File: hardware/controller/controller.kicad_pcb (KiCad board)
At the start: 4 copper layers, 100 x 60 mm, 210 parts, among them J1 USB_C_Receptacle_USB2.0_14P, J10 Conn_01x01, J11 Conn_01x01, J12 Conn_01x01, J13 Conn_01x06, J14 Conn_01x03, J15 Mini-SPOX, J16 Mini-SPOX, J2 IDC-10, J3 XT-60, J4 Conn_01x07, J5 Conn_01x01, J6 Conn_01x01, J7 Conn_01x01, J8 Conn_01x06, J9 Conn_01x03, Q1 AOD4189, Q10 AOD66406, Q11 AOD66406, Q12 AOD66406, Q13 AOD66406, Q2 AOD66406, Q3 AOD66406, Q4 AOD66406, Q5 AOD66406, Q6 AOD66406, Q7 AOD66406, Q8 AOD66406, Q9 AOD66406, SW1 SW_Push, SW2 SW_SPST, U1 USBLC6-2SC6, U10 MCP6541, U11 LM2105D, U12 MCP6541, U13 LM2105D, U14 MCP6541, U15 LM2105D, U16 MCP6541, U17 LM2105D, U18 MCP6541, U19 LM2105D, U2 STM32H523RETx, U20 TXS0101DBV, U21 TXS0101DBV, U3 ESP32-C3-WROOM-02, U4 LM1117MP-3.3, U5 LV14340, U6 MPU-6050, U7 HMC5883L, U8 MCP6541, U9 LM2105D, Y1 8MHz

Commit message: wip - placement
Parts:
- removed J15, J16: Mini-SPOX, hogger2:Molex-MiniSPOX-22057035-5268
- C10, C11, C12, C13, C14, C15, C21, C22, C23, C24, C25, C26, C27, C28, C29, C36, C37, C38, C39, C40, C41, C42, C44, C45, C46, C47, C49, C50, C51, C52, C54, C55, C56, C57, C59, C60, C61, C62, C64, C65, C66, C67, C69, C70, C73, C74, D3, JP1, JP2, JP3, JP4, JP5, JP6, L1, R10, R12, R14, R15, R16, R20, R21, R22, R23, R24, R25, R26, R27, R28, R29, R30, R31, R32, R33, R34, R35, R36, R37, R38, R39, R40, R41, R42, R43, R44, R45, R46, R47, R48, R49, R50, R51, R52, R53, R54, R55, R56, R57, R58, R59, R60, R61, R62, R63, U10, U11, U12, U13, U14, U15, U16, U17, U18, U19, U20, U21, U3, U4, U5, U7, U8, U9: moved to B.Cu
- J12: value Conn_01x01 -> Conn_01x09; footprint Connector_Wire:SolderWire-2.5sqmm_1x01_D2.4mm_OD4.4mm -> Connector_PinHeader_2.54mm:PinHeader_1x09_P2.54mm_Vertical
- J13: value Conn_01x06 -> Mini-SPOX; footprint Connector_PinHeader_2.54mm:PinHeader_1x06_P2.54mm_Vertical -> hogger2:Molex-MiniSPOX-22057035-5268
- J14: value Conn_01x03 -> Mini-SPOX; footprint Connector_PinHeader_2.54mm:PinHeader_1x03_P2.54mm_Vertical -> hogger2:Molex-MiniSPOX-22057035-5268
- J8: value Conn_01x06 -> Conn_01x09; footprint Connector_PinHeader_2.54mm:PinHeader_1x06_P2.54mm_Vertical -> Connector_PinHeader_2.54mm:PinHeader_1x09_P2.54mm_Vertical
- J9: value Conn_01x03 -> Conn_01x01; footprint Connector_PinHeader_2.54mm:PinHeader_1x03_P2.54mm_Vertical -> Connector_Wire:SolderWire-2.5sqmm_1x01_D2.4mm_OD4.4mm
- moved U7 176.1 mm to (146.5, 53.5)
- moved C69 173.0 mm to (131.2, 107.0), turned to 90 degrees
- moved C70 173.0 mm to (131.2, 111.0), turned to -90 degrees
- moved R21 171.9 mm to (141.5, 55.5), turned to 180 degrees
- moved R20 169.6 mm to (141.5, 57.5), turned to 180 degrees
- moved C36 168.1 mm to (141.5, 53.5), turned to 180 degrees
- moved J13 168.1 mm to (135.5, 113.5)
- moved C72 167.3 mm to (137.0, 109.5)
- moved C37 162.0 mm to (150.5, 53.2), turned to -90 degrees
- moved C38 161.3 mm to (152.5, 54.0), turned to -90 degrees
- moved U20 161.1 mm to (134.2, 109.0), turned to -90 degrees
- moved C73 144.6 mm to (160.0, 107.0), turned to 90 degrees
- moved C74 144.5 mm to (160.0, 111.0), turned to -90 degrees
- moved JP1 142.8 mm to (111.5, 85.5), turned to 90 degrees
- moved U8 141.7 mm to (107.5, 87.5), turned to 90 degrees
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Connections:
- J10 pad 1: /motor2/PHASE_U -> /motor2/PHASE_V
- J11 pad 1: /motor2/PHASE_V -> /motor2/PHASE_W
- J12 pad 1: /motor2/PHASE_W -> MOTOR2_PWM_UH
- J13 pad 1: MOTOR2_PWM_UH -> GND
- J13 pad 2: MOTOR2_PWM_UL -> VBUS
- J13 pad 3: MOTOR2_PWM_VH -> /servos/SERVO1_TTL
- J14 pad 1: MOTOR2_BEMF_U -> GND
- J14 pad 2: MOTOR2_BEMF_V -> VBUS
- J14 pad 3: MOTOR2_BEMF_W -> /servos/SERVO2_TTL
- J9 pad 1: MOTOR1_BEMF_U -> /motor2/PHASE_U
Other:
- board size 100 x 60 mm -> 100 x 70 mm
- board text added: "Hogger^2 Controller V1.1 by Eryk Możdżeń March 2025"
- board text removed: "Hogger^2 Controller V1.0 by Eryk Możdżeń November 2024"

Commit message: wip elements
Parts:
- C21: value 100n/16V -> 100n/50V
- C32: value 10u -> 10u/50V; footprint Capacitor_SMD:C_0603_1608Metric -> Capacitor_SMD:C_1206_3216Metric
- C35: value 2n2 -> 2.2n
- Q1: value AOD4189 -> DMPH4013SK3
- Q10, Q11, Q12, Q13, Q2, Q3, Q4, Q5, Q6, Q7, Q8, Q9: value AOD66406 -> IPD90N04S4L04
- moved C32 0.79 mm to (170.5, 64.0)

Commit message: wip routing power stages
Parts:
- moved JP4 7.52 mm to (173.0, 86.0), turned to -90 degrees
- moved JP1 7.52 mm to (104.0, 86.0), turned to -90 degrees
- moved JP2 7.52 mm to (112.0, 86.0), turned to -90 degrees
- moved JP3 7.52 mm to (120.0, 86.0), turned to -90 degrees
- moved JP5 7.52 mm to (181.0, 86.0), turned to -90 degrees
- moved JP6 7.52 mm to (189.0, 86.0), turned to -90 degrees
- moved R22 4.03 mm to (104.0, 93.0), turned to 0 degrees
- moved R28 4.03 mm to (112.0, 93.0), turned to 0 degrees
- moved R37 4.03 mm to (120.0, 93.0), turned to 0 degrees
- moved R49 4.03 mm to (181.0, 93.0), turned to 0 degrees
- moved R58 4.03 mm to (189.0, 93.0), turned to 0 degrees
- moved R43 4.01 mm to (173.0, 93.0), turned to 0 degrees
- moved C27 3.26 mm to (166.5, 91.0)
- moved C28 3.26 mm to (166.5, 95.0)
- moved C26 1.77 mm to (143.5, 94.0), turned to -90 degrees
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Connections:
- J12 pad 1: MOTOR2_PWM_UH -> MOTOR2_BEMF_U
- J12 pad 2: MOTOR2_PWM_UL -> MOTOR2_PWM_UH
- J12 pad 3: MOTOR2_PWM_VH -> MOTOR2_PWM_UL
- J12 pad 4: MOTOR2_PWM_VL -> MOTOR2_BEMF_V
- J12 pad 5: MOTOR2_PWM_WH -> MOTOR2_PWM_VH
- J12 pad 6: MOTOR2_PWM_WL -> MOTOR2_PWM_VL
- J12 pad 7: MOTOR2_BEMF_U -> MOTOR2_BEMF_W
- J12 pad 8: MOTOR2_BEMF_V -> MOTOR2_PWM_WH
- J12 pad 9: MOTOR2_BEMF_W -> MOTOR2_PWM_WL
- J8 pad 1: MOTOR1_PWM_UH -> MOTOR1_BEMF_U
- J8 pad 2: MOTOR1_PWM_UL -> MOTOR1_PWM_UH
- J8 pad 3: MOTOR1_PWM_VH -> MOTOR1_PWM_UL
- J8 pad 4: MOTOR1_PWM_VL -> MOTOR1_BEMF_V
- J8 pad 5: MOTOR1_PWM_WH -> MOTOR1_PWM_VH
- J8 pad 6: MOTOR1_PWM_WL -> MOTOR1_PWM_VL
- J8 pad 7: MOTOR1_BEMF_U -> MOTOR1_BEMF_W
- J8 pad 8: MOTOR1_BEMF_V -> MOTOR1_PWM_WH
- J8 pad 9: MOTOR1_BEMF_W -> MOTOR1_PWM_WL
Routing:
- net GND: track 0.00 -> 122.1 mm, vias 0 -> 207
- net +3.3V: track 0.00 -> 119.6 mm, vias 0 -> 6
- net VBUS: track 0.00 -> 75.9 mm, vias 0 -> 16
- net /motor1/PHASE_U: track 0.00 -> 37.5 mm, vias 0 -> 2
- net /motor1/PHASE_V: track 0.00 -> 36.9 mm, vias 0 -> 2
- net /motor2/PHASE_V: track 0.00 -> 36.8 mm, vias 0 -> 2
- net /motor1/PHASE_W: track 0.00 -> 36.5 mm, vias 0 -> 2
- net /motor2/PHASE_U: track 0.00 -> 36.4 mm, vias 0 -> 2
- net /motor2/PHASE_W: track 2.83 -> 37.4 mm, vias 0 -> 2
- net /motor2/BEMF_ZERO: track 0.00 -> 31.2 mm, vias 0 -> 3
- net /motor1/BEMF_ZERO: track 0.00 -> 31.1 mm, vias 0 -> 3
- net MOTOR2_PWM_WH: track 0.00 -> 29.4 mm
- net MOTOR1_PWM_VH: track 0.00 -> 29.1 mm
- net MOTOR1_PWM_WH: track 0.00 -> 29.0 mm
- net MOTOR2_PWM_VH: track 0.00 -> 28.6 mm
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- added copper zone on In1.Cu, net +3.3V
- added copper zone on B.Cu, net +5V
- added copper zone on F.Cu, net /power/BATTERY_IN
- added copper zone on B.Cu, net GND
- added copper zone on F.Cu, net GND
- added copper zone on In1.Cu, net GND
- added copper zone on In2.Cu, net GND
- added copper zone on B.Cu, net Net-(D3-K)
- added copper zone on B.Cu, net VBUS
- added copper zone on F.Cu, net VBUS

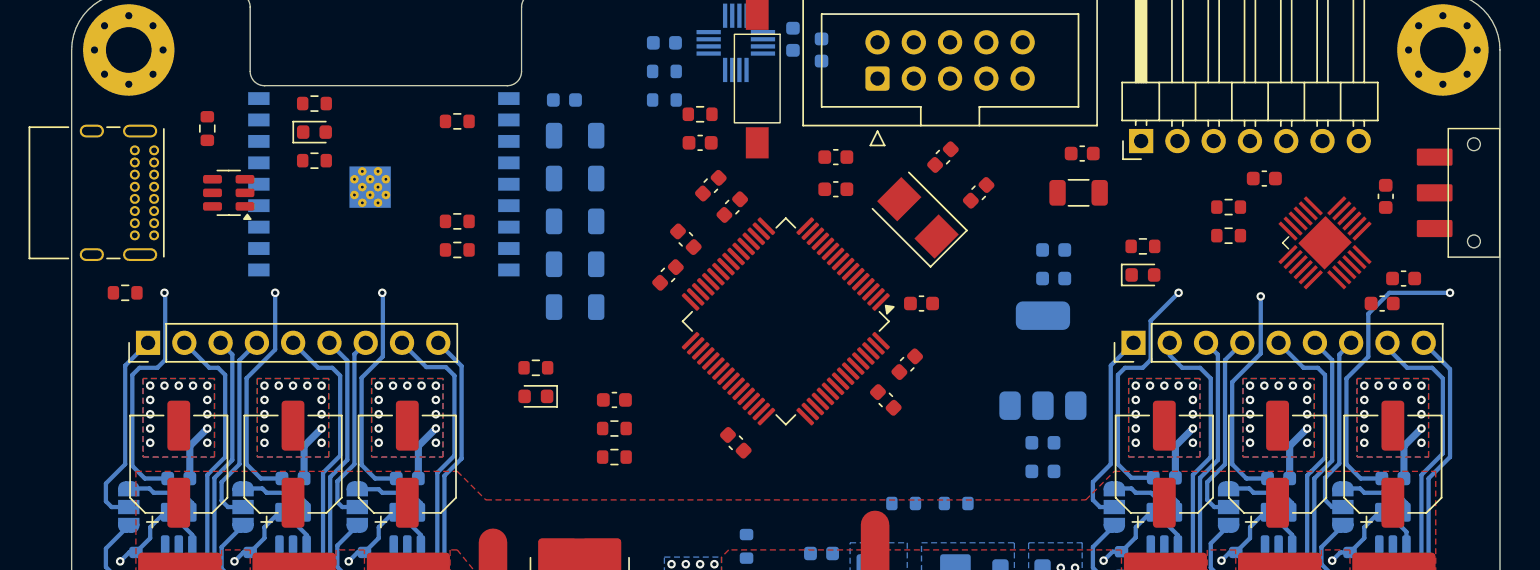
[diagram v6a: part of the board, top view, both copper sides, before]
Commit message: wip - motor and ESP signals
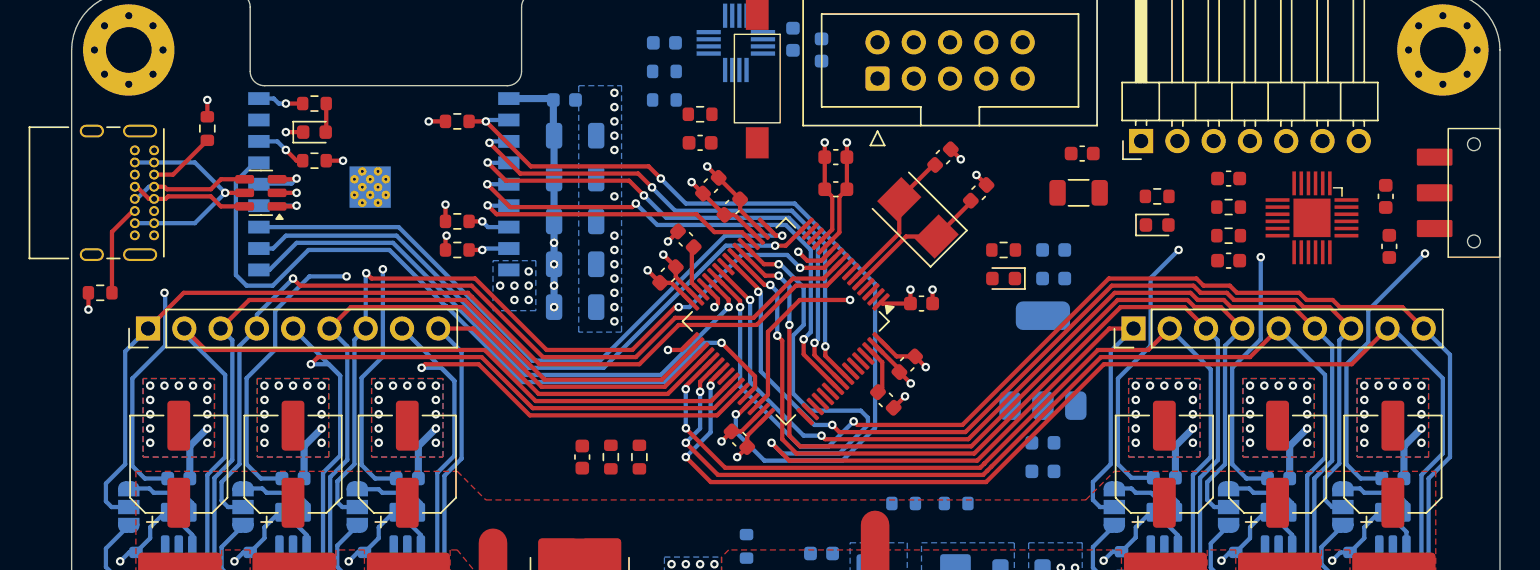
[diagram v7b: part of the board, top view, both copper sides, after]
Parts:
- moved D2 33.8 mm to (165.2, 70.0)
- moved R9 33.8 mm to (165.2, 68.0)
- moved C34 12.3 mm to (181.0, 68.8)
- moved C20 4.59 mm to (135.8, 82.5), turned to -90 degrees
- moved C30 4.03 mm to (192.2, 67.8), turned to 90 degrees
- moved D4 3.64 mm to (176.0, 66.2)
- moved R17 3.64 mm to (176.0, 64.2)
- moved C35 2.50 mm to (181.0, 63.0)
- moved U1 2.25 mm to (113.2, 64.0)
- moved R13 2.02 mm to (137.8, 82.5), turned to -90 degrees
- moved U6 1.97 mm to (186.8, 65.8), turned to -90 degrees
- moved R11 1.75 mm to (139.8, 82.5), turned to 90 degrees
- moved R2 1.75 mm to (102.0, 71.0), turned to 180 degrees
- moved J12 1.00 mm to (174.3, 73.5)
- moved J8 1.00 mm to (105.3, 73.5)
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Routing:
- net MOTOR2_PWM_WL: track 27.2 -> 92.7 mm, vias 0 -> 2
- net MOTOR2_PWM_WH: track 29.4 -> 90.9 mm, vias 0 -> 2
- net +3.3V: track 119.6 -> 180.2 mm, vias 6 -> 20
- net /microcontroller/ESP_EN: track 0.00 -> 59.1 mm, vias 0 -> 3
- net MOTOR2_BEMF_W: track 13.2 -> 71.3 mm, vias 0 -> 2
- net MOTOR2_BEMF_U: track 13.9 -> 71.9 mm, vias 0 -> 2
- net MOTOR2_PWM_VL: track 26.8 -> 82.9 mm, vias 0 -> 2
- net MOTOR1_BEMF_U: track 14.1 -> 69.9 mm
- net /microcontroller/ESP_HANDSHAKE: track 0.00 -> 54.0 mm, vias 0 -> 1
- net MOTOR2_PWM_VH: track 28.6 -> 81.9 mm, vias 0 -> 2
- net MOTOR2_BEMF_V: track 13.7 -> 66.7 mm, vias 0 -> 2
- net MOTOR2_PWM_UL: track 26.7 -> 77.0 mm, vias 0 -> 2
- net MOTOR1_BEMF_V: track 13.8 -> 62.7 mm, vias 0 -> 1
- net GND: track 122.1 -> 169.1 mm, vias 207 -> 240
- net /microcontroller/ESP_RXD: track 0.00 -> 46.6 mm, vias 0 -> 1
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
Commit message: wip better pinout
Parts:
- C20, R11, R13: moved to B.Cu
- moved D2 21.7 mm to (143.7, 72.8), turned to 0 degrees
- moved R9 21.7 mm to (143.8, 70.9)
- moved C16 18.4 mm to (145.8, 59.2), turned to 135 degrees
- moved C17 17.8 mm to (143.2, 61.8), turned to 135 degrees
- moved C4 16.5 mm to (162.0, 75.0), turned to -135 degrees
- moved C3 15.3 mm to (151.5, 81.5), turned to 135 degrees
- moved C19 14.3 mm to (149.0, 80.2), turned to -135 degrees
- moved C18 13.9 mm to (159.2, 64.8), turned to 45 degrees
- moved C8 13.1 mm to (142.2, 68.2), turned to 90 degrees
- moved C5 12.9 mm to (156.8, 63.2), turned to -45 degrees
- moved C1 12.1 mm to (142.5, 75.4), turned to 90 degrees
- moved Y1 12.0 mm to (147.5, 63.5), turned to -135 degrees
- moved C6 11.8 mm to (152.5, 62.2), turned to 90 degrees
- moved C2 10.5 mm to (144.5, 75.4), turned to 90 degrees
- moved C7 10.1 mm to (144.5, 68.2), turned to 90 degrees
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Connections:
- U2 pad 10: MOTOR1_BEMF_W -> MOTOR2_BEMF_W
- U2 pad 2: FLOW_INT -> unconnected-(U2-PC13-Pad2)
- U2 pad 21: MOTOR2_BEMF_U -> MOTOR1_BEMF_U
- U2 pad 22: MOTOR2_BEMF_V -> MOTOR1_BEMF_V
- U2 pad 23: MOTOR2_PWM_UL -> MOTOR1_PWM_UL
- U2 pad 24: MOTOR2_BEMF_W -> MOTOR1_BEMF_W
- U2 pad 26: MOTOR2_PWM_VL -> MOTOR1_PWM_VL
- U2 pad 27: MOTOR2_PWM_WL -> MOTOR1_PWM_WL
- U2 pad 29: MAG_SCL -> IMU_SCL
- U2 pad 3: IMU_INT -> unconnected-(U2-PC14-Pad3)
- U2 pad 33: MAG_SDA -> IMU_SDA
- U2 pad 34: MOTOR1_PWM_UL -> MOTOR2_PWM_UL
- U2 pad 35: MOTOR1_PWM_VL -> MOTOR2_PWM_VL
- U2 pad 36: MOTOR1_PWM_WL -> MOTOR2_PWM_WL
- U2 pad 37: MOTOR2_PWM_UH -> MOTOR1_PWM_UH
- U2 pad 38: MOTOR2_PWM_VH -> MOTOR1_PWM_VH
- U2 pad 39: MOTOR2_PWM_WH -> MOTOR1_PWM_WH
- U2 pad 40: unconnected-(U2-PC9-Pad40) -> IMU_INT
- U2 pad 41: MOTOR1_PWM_UH -> MOTOR2_PWM_UH
- U2 pad 42: MOTOR1_PWM_VH -> MOTOR2_PWM_VH
- U2 pad 43: MOTOR1_PWM_WH -> MOTOR2_PWM_WH
- U2 pad 54: unconnected-(U2-PD2-Pad54) -> FLOW_INT
- U2 pad 58: IMU_SCL -> MAG_SCL
- U2 pad 59: IMU_SDA -> MAG_SDA
- U2 pad 8: MOTOR1_BEMF_U -> MOTOR2_BEMF_U
- U2 pad 9: MOTOR1_BEMF_V -> MOTOR2_BEMF_V
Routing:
- net FLOW_INT: track 0.00 -> 35.3 mm
- net FLOW_MOSI: track 0.00 -> 33.7 mm, vias 0 -> 1
- net FLOW_MISO: track 0.00 -> 31.6 mm
- net IMU_SCL: track 0.00 -> 29.5 mm, vias 0 -> 2
- net IMU_SDA: track 0.00 -> 28.8 mm, vias 0 -> 2
- net FLOW_CS: track 0.00 -> 27.1 mm, vias 0 -> 2
- net FLOW_SCK: track 0.00 -> 25.9 mm
- net IMU_INT: track 0.00 -> 24.4 mm, vias 0 -> 2
- net MOTOR2_BEMF_U: track 71.9 -> 48.2 mm
- net VBUS_SENSE: track 2.78 -> 26.2 mm
- net MOTOR2_PWM_WH: track 90.9 -> 67.5 mm, vias 2 -> 0
- net MOTOR2_PWM_VH: track 81.9 -> 60.0 mm, vias 2 -> 0
- net MOTOR2_PWM_WL: track 92.7 -> 70.8 mm, vias 2 -> 0
- net /microcontroller/STM_SWCLK: track 0.00 -> 21.5 mm, vias 0 -> 2
- net MOTOR1_PWM_UH: track 69.9 -> 90.7 mm, vias 0 -> 2
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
